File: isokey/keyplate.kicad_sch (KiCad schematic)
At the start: 164 parts

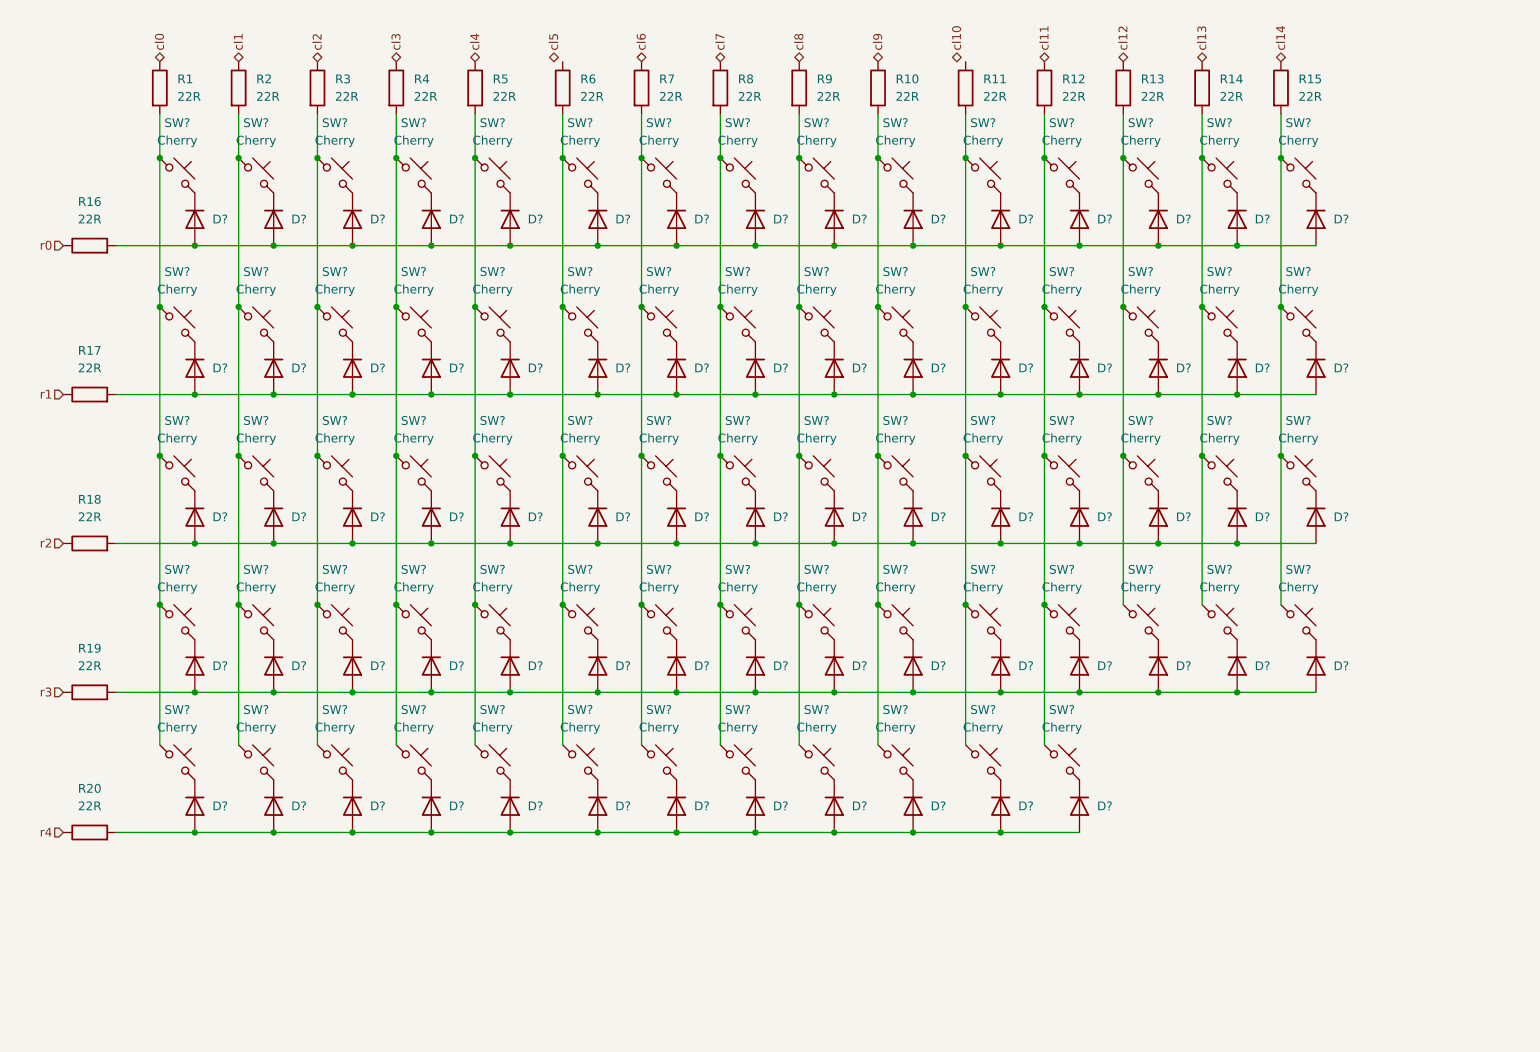
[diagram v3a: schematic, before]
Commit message: Complete led wire
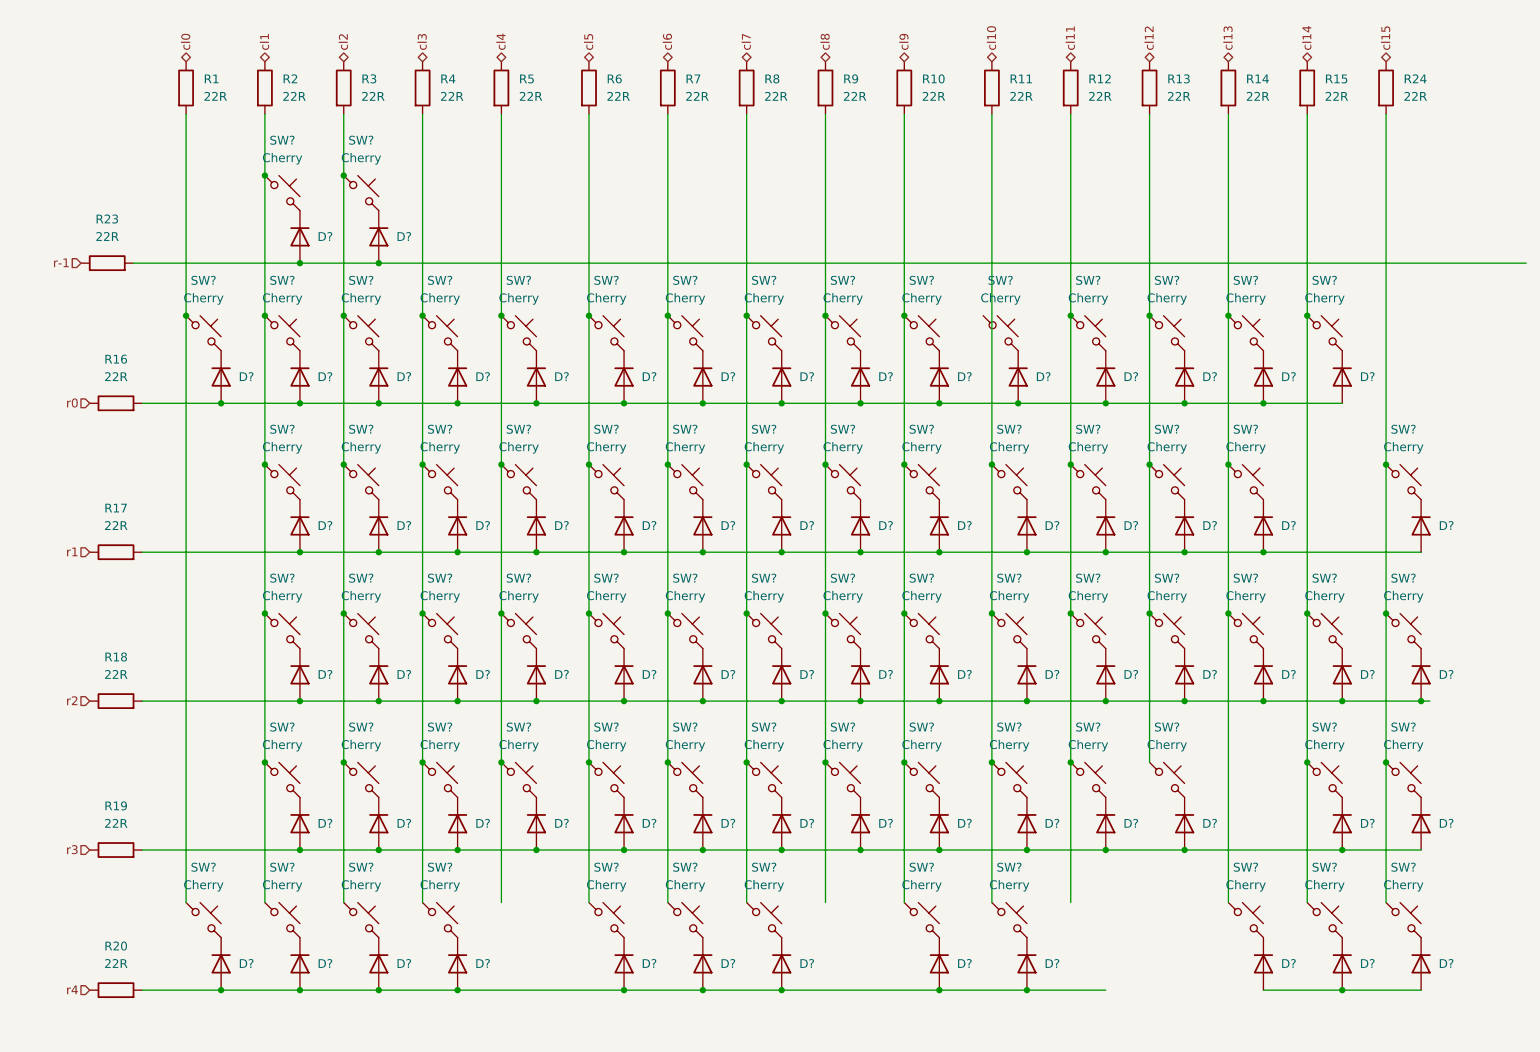
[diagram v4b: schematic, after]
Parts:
- added R23, R24: 22R, Resistor_SMD:R_0603_1608Metric_Pad0.98x0.95mm_HandSolder, symbol Device:R
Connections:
- net cl10: now also R11.1
- net cl5: now also R6.1
- net at R7.2, SW?.1, SW?.1: now also SW?.1, SW?.1, SW?.1; no longer SW?.1, SW?.1, SW?.1
- net at D?.2 (A), D?.2 (A), D?.2 (A)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: now also D?.2 (A); no longer D?.2 (A), D?.2 (A)
- net at R4.2, SW?.1, SW?.1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: now also SW?.1, SW?.1; no longer SW?.1, SW?.1
- net at R5.2, SW?.1, SW?.1: now also SW?.1, SW?.1; no longer SW?.1, SW?.1, SW?.1
- net at D?.2 (A), D?.2 (A), D?.2 (A)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: now also D?.2 (A), D?.2 (A); no longer D?.2 (A), D?.2 (A)
- net at D?.2 (A), D?.2 (A), D?.2 (A)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: no longer D?.2 (A), D?.2 (A), D?.2 (A)
- net at R11.2, SW?.1, SW?.1: now also SW?.1, SW?.1; no longer SW?.1, SW?.1, SW?.1
- net at R2.2, SW?.1, SW?.1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: now also SW?.1, SW?.1, SW?.1; no longer SW?.1, SW?.1
- net at D?.2 (A), D?.2 (A), D?.2 (A)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: no longer D?.2 (A)
- net at R9.2, SW?.1, SW?.1: now also SW?.1, SW?.1; no longer SW?.1, SW?.1, SW?.1
- net at R12.2, SW?.1, SW?.1: now also SW?.1, SW?.1; no longer SW?.1, SW?.1, SW?.1
- net at D?.2 (A), D?.2 (A), D?.2 (A)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: now also D?.2 (A); no longer D?.2 (A)
- net at R8.2, SW?.1, SW?.1: now also SW?.1, SW?.1, SW?.1; no longer SW?.1, SW?.1, SW?.1
- net at R6.2, SW?.1, SW?.1: now also SW?.1, SW?.1, SW?.1; no longer SW?.1, SW?.1, SW?.1
- net at R3.2, SW?.1, SW?.1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: now also SW?.1, SW?.1, SW?.1; no longer SW?.1, SW?.1
- net at R10.2, SW?.1, SW?.1: now also SW?.1, SW?.1, SW?.1; no longer SW?.1, SW?.1, SW?.1
- net at R13.2, SW?.1, SW?.1: now also SW?.1, SW?.1; no longer SW?.1, SW?.1
- new net: R24.2, SW?.1, SW?.1, SW?.1, SW?.1
- new net: D?.2 (A), D?.2 (A), D?.2 (A)
- new net: R14.2, SW?.1, SW?.1, SW?.1, SW?.1
- new net: R15.2, SW?.1, SW?.1, SW?.1, SW?.1
- new net: R1.2, SW?.1, SW?.1
- new net: D?.2 (A), D?.2 (A), R23.2
- new net cl15: R24.1
- new net r-1: R23.1
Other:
- moved on the sheet: D?, R1, R10, R11, R12, R13, R14, R15, R16, R17, R18, R19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

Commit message: Continue routing
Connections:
- net at D?.2 (A), D?.2 (A), D?.2 (A)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: now also D?.2 (A), D?.2 (A), D?.2 (A)
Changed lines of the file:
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@@
   (junction (at 115.57 162.56) (diameter 0) (color 0 0 0 0)
+  )
+  (junction (at 208.28 162.56) (diameter 0) (color 0 0 0 0)
   )
   (wire (pts (xy 68.58 57.15) (xy 80.01 57.15))
@@
     (stroke (width 0) (type default))
   )
-  (wire (pts (xy 173.99 162.56) (xy 185.42 162.56))
+  (wire (pts (xy 173.99 162.56) (xy 208.28 162.56))
     (stroke (width 0) (type default))
   )

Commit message: Continue routing
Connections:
- net at R11.2, SW?.1, SW?.1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: now also SW?.1
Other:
- moved on the sheet: D?, SW?
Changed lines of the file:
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@@
   (junction (at 156.21 64.77) (diameter 0) (color 0 0 0 0)
   )
-  (junction (at 172.72 77.47) (diameter 0) (color 0 0 0 0)
-  )
   (junction (at 138.43 99.06) (diameter 0) (color 0 0 0 0)
   )
@@
   (junction (at 161.29 142.24) (diameter 0) (color 0 0 0 0)
   )
+  (junction (at 173.99 77.47) (diameter 0) (color 0 0 0 0)
+  )
   (junction (at 203.2 86.36) (diameter 0) (color 0 0 0 0)
   )
@@
   (junction (at 133.35 86.36) (diameter 0) (color 0 0 0 0)
   )
+  (junction (at 168.91 64.77) (diameter 0) (color 0 0 0 0)
+  )
   (junction (at 80.01 120.65) (diameter 0) (color 0 0 0 0)
   )
@@
   (junction (at 208.28 162.56) (diameter 0) (color 0 0 0 0)
   )
+  (wire (pts (xy 173.99 77.47) (xy 185.42 77.47))
+    (stroke (width 0) (type default))
+  )
   (wire (pts (xy 68.58 57.15) (xy 80.01 57.15))
     (stroke (width 0) (type default))
@@
     (stroke (width 0) (type default))
   )
-  (wire (pts (xy 172.72 77.47) (xy 185.42 77.47))
-    (stroke (width 0) (type default))
-  )
   (wire (pts (xy 133.35 64.77) (xy 133.35 86.36))
     (stroke (width 0) (type default))
@@
     (stroke (width 0) (type default))
   )
-  (wire (pts (xy 161.29 77.47) (xy 172.72 77.47))
+  (wire (pts (xy 161.29 77.47) (xy 173.99 77.47))
     (stroke (width 0) (type default))
   )
@@
     (stroke (width 0) (type default))
   )
-  (wire (pts (xy 168.91 35.56) (xy 168.91 86.36))
+  (wire (pts (xy 168.91 35.56) (xy 168.91 64.77))
     (stroke (width 0) (type default))
   )
@@
     (stroke (width 0) (type default))
   )
+  (wire (pts (xy 168.91 64.77) (xy 168.91 86.36))
+    (stroke (width 0) (type default))
+  )
   (wire (pts (xy 102.87 77.47) (xy 115.57 77.47))
     (stroke (width 0) (type default))
@@
     )
   )
-  (symbol (lib_id "Diode:1N4448W") (at 172.72 73.66 270) (unit 1)
+  (symbol (lib_id "Diode:1N4448W") (at 173.99 73.66 270) (unit 1)
     (in_bom yes) (on_board yes) (dnp no) (fields_autoplaced)
-    (property "Reference" "D?" (at 175.26 73.66 90)
+    (property "Reference" "D?" (at 176.53 73.66 90)
       (effects (font (size 1.27 1.27)) (justify left))
     )
-    (property "Value" "1N4448W" (at 175.26 74.93 90)
+    (property "Value" "1N4448W" (at 176.53 74.93 90)
       (effects (font (size 1.27 1.27)) (justify left) hide)
     )
-    (property "Footprint" "Diode_SMD:D_SOD-123" (at 168.275 73.66 0)
+    (property "Footprint" "Diode_SMD:D_SOD-123" (at 169.545 73.66 0)
       (effects (font (size 1.27 1.27)) hide)
     )
-    (property "Datasheet" "https://www.vishay.com/docs/85722/1n4448w.pdf" (at 172.72 73.66 0)
+    (property "Datasheet" "https://www.vishay.com/docs/85722/1n4448w.pdf" (at 173.99 73.66 0)
       (effects (font (size 1.27 1.27)) hide)
     )
-    (property "Sim.Device" "D" (at 172.72 73.66 0)
+    (property "Sim.Device" "D" (at 173.99 73.66 0)
       (effects (font (size 1.27 1.27)) hide)
     )
-    (property "Sim.Pins" "1=K 2=A" (at 172.72 73.66 0)
+    (property "Sim.Pins" "1=K 2=A" (at 173.99 73.66 0)
       (effects (font (size 1.27 1.27)) hide)
     )
@@
     )
   )
-  (symbol (lib_id "Switch:SW_Push_45deg") (at 170.18 67.31 0) (unit 1)
+  (symbol (lib_id "Switch:SW_Push_45deg") (at 171.45 67.31 0) (unit 1)
     (in_bom yes) (on_board yes) (dnp no) (fields_autoplaced)
-    (property "Reference" "SW?" (at 170.18 59.69 0)
+    (property "Reference" "SW?" (at 171.45 59.69 0)
       (effects (font (size 1.27 1.27)))
     )
-    (property "Value" "Cherry" (at 170.18 62.23 0)
+    (property "Value" "Cherry" (at 171.45 62.23 0)
       (effects (font (size 1.27 1.27)))
     )
-    (property "Footprint" "Button_Switch_Keyboard:Kailh_socket_MX_LED" (at 170.18 67.31 0)
+    (property "Footprint" "Button_Switch_Keyboard:Kailh_socket_MX_LED" (at 171.45 67.31 0)
       (effects (font (size 1.27 1.27)) hide)
     )
-    (property "Datasheet" "~" (at 170.18 67.31 0)
+    (property "Datasheet" "~" (at 171.45 67.31 0)
       (effects (font (size 1.27 1.27)) hide)
     )

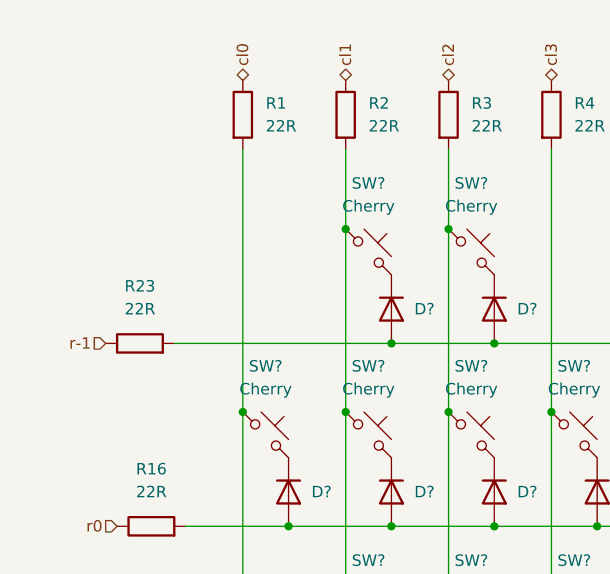
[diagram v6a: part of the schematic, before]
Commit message: Add lp5569 chip and encoder.
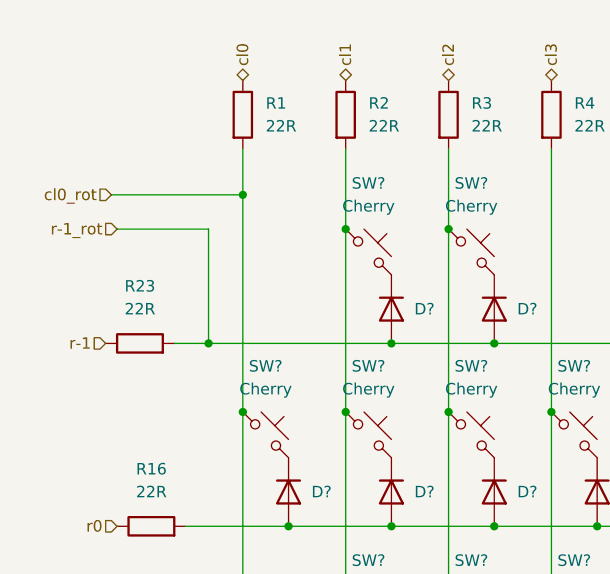
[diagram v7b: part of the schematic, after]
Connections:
- net cl0_rot: now reaches R1.2, SW?.1, SW?.1
- net r-1_rot: now reaches D?.2 (A), D?.2 (A), R23.2
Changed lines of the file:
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@@
   (junction (at 180.34 86.36) (diameter 0) (color 0 0 0 0)
   )
+  (junction (at 48.26 57.15) (diameter 0) (color 0 0 0 0)
+  )
   (junction (at 80.01 57.15) (diameter 0) (color 0 0 0 0)
   )
@@
   (junction (at 86.36 86.36) (diameter 0) (color 0 0 0 0)
   )
+  (junction (at 52.07 40.64) (diameter 0) (color 0 0 0 0)
+  )
   (junction (at 91.44 162.56) (diameter 0) (color 0 0 0 0)
   )
@@
   (junction (at 208.28 162.56) (diameter 0) (color 0 0 0 0)
   )
+  (wire (pts (xy 48.26 57.15) (xy 48.26 44.45))
+    (stroke (width 0) (type default))
+  )
   (wire (pts (xy 173.99 77.47) (xy 185.42 77.47))
     (stroke (width 0) (type default))
@@
     (stroke (width 0) (type default))
   )
-  (wire (pts (xy 44.45 57.15) (xy 68.58 57.15))
+  (wire (pts (xy 44.45 57.15) (xy 48.26 57.15))
     (stroke (width 0) (type default))
   )
@@
     (stroke (width 0) (type default))
   )
+  (wire (pts (xy 52.07 40.64) (xy 52.07 64.77))
+    (stroke (width 0) (type default))
+  )
   (wire (pts (xy 63.5 35.56) (xy 63.5 44.45))
     (stroke (width 0) (type default))
@@
     (stroke (width 0) (type default))
   )
+  (wire (pts (xy 38.1 44.45) (xy 48.26 44.45))
+    (stroke (width 0) (type default))
+  )
   (wire (pts (xy 191.77 64.77) (xy 191.77 86.36))
     (stroke (width 0) (type default))
@@
     (stroke (width 0) (type default))
   )
+  (wire (pts (xy 48.26 57.15) (xy 68.58 57.15))
+    (stroke (width 0) (type default))
+  )
   (wire (pts (xy 86.36 86.36) (xy 86.36 107.95))
     (stroke (width 0) (type default))
@@
     (stroke (width 0) (type default))
   )
-  (wire (pts (xy 52.07 35.56) (xy 52.07 64.77))
+  (wire (pts (xy 52.07 35.56) (xy 52.07 40.64))
     (stroke (width 0) (type default))
   )
@@
     (stroke (width 0) (type default))
   )
+  (wire (pts (xy 37.465 40.64) (xy 52.07 40.64))
+    (stroke (width 0) (type default))
+  )
   (wire (pts (xy 203.2 35.56) (xy 203.2 64.77))
     (stroke (width 0) (type default))
@@
   (hierarchical_label "cl0" (shape bidirectional) (at 52.07 27.94 90) (fields_autoplaced)
     (effects (font (size 1.27 1.27)) (justify left))
+  )
+  (hierarchical_label "r-1_rot" (shape input) (at 38.1 44.45 180) (fields_autoplaced)
+    (effects (font (size 1.27 1.27)) (justify right))
   )
   (hierarchical_label "r1" (shape input) (at 38.1 99.06 180) (fields_autoplaced)
@@
     (effects (font (size 1.27 1.27)) (justify left))
   )
+  (hierarchical_label "cl0_rot" (shape input) (at 37.465 40.64 180) (fields_autoplaced)
+    (effects (font (size 1.27 1.27)) (justify right))
+  )
   (hierarchical_label "cl14" (shape bidirectional) (at 214.63 27.94 90) (fields_autoplaced)
